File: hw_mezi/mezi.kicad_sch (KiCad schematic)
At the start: 39 parts, among them J1 Conn_2Rows-05Pins, Q1 AO3401A, Q2 AO3401A, Q3 AO3401A, SW1 SW_DPST_x2, T1 Tab, U1 PY32F002AF15P6TU

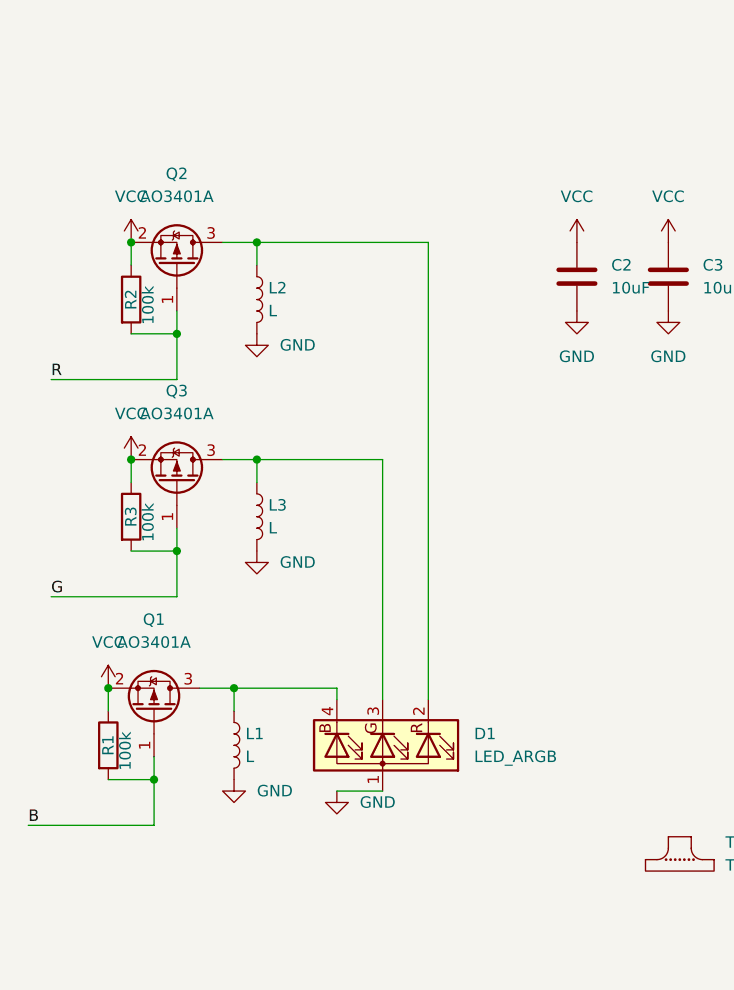
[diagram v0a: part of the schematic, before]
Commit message: Hoember + Mezi routed
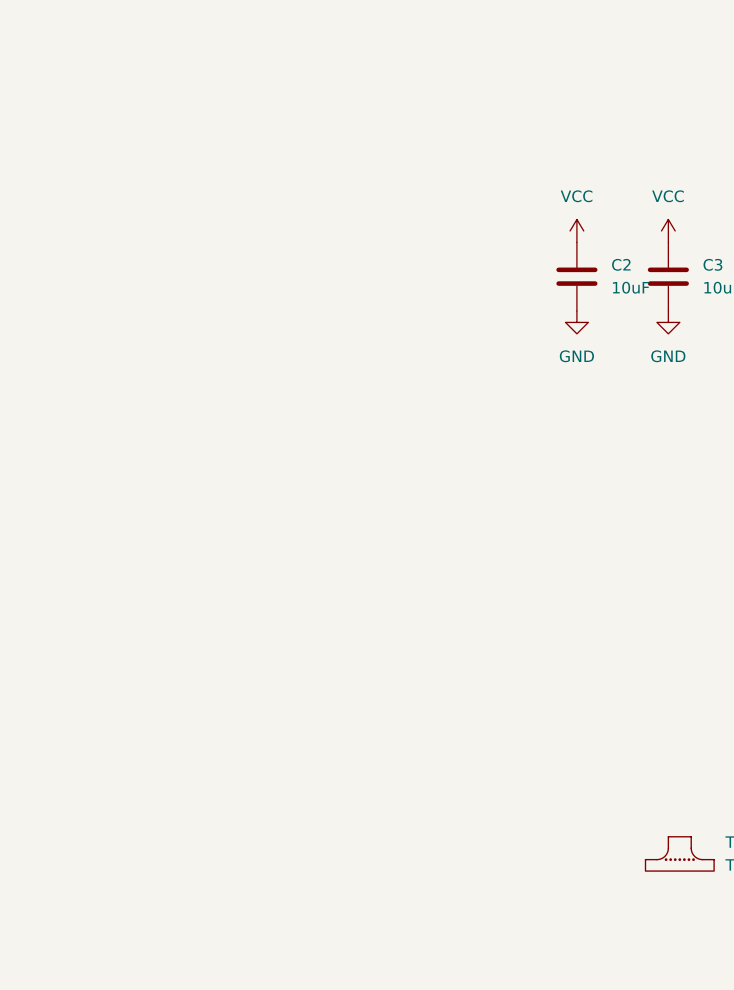
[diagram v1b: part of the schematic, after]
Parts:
- removed D1: LED_ARGB, LED_SMD:LED_RGB_Wuerth-PLCC4_3.2x2.8mm_150141M173100, symbol Device:LED_ARGB
- removed L1, L2, L3: L, Inductor_SMD:L_1008_2520Metric, symbol Device:L
- removed Q1, Q2, Q3: AO3401A, karifa:SOT-23, symbol Transistor_FET:AO3401A
- removed R1, R2, R3: 100k, Resistor_SMD:R_0603_1608Metric, symbol Device:R

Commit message: mezi tssop JLC swap + hole on top
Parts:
- U1: footprint Package_SO:TSSOP-20_4.4x6.5mm_P0.65mm -> karifa:TSSOP-20_4.4x6.5mm_P0.65mm
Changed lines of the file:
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@@
       (effects (font (size 1.27 1.27)))
     )
-    (property "Footprint" "Package_SO:TSSOP-20_4.4x6.5mm_P0.65mm" (at 187.96 104.14 0)
+    (property "Footprint" "karifa:TSSOP-20_4.4x6.5mm_P0.65mm" (at 187.96 104.14 0)
       (effects (font (size 1.27 1.27)) hide)
     )
